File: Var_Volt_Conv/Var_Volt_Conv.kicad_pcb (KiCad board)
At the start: 6 copper layers, 101 x 65 mm, 101 parts, among them J101 Jack-DC, J102 Screw_Terminal_01x02, J103 Screw_Terminal_01x02, J201 Conn_01x05, Q101 AO3416, Q102 IRFML8244TRPBF, Q103 IRFML8244TRPBF, Q104 AO3407, Q105 AO3407, Q106 AO3407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

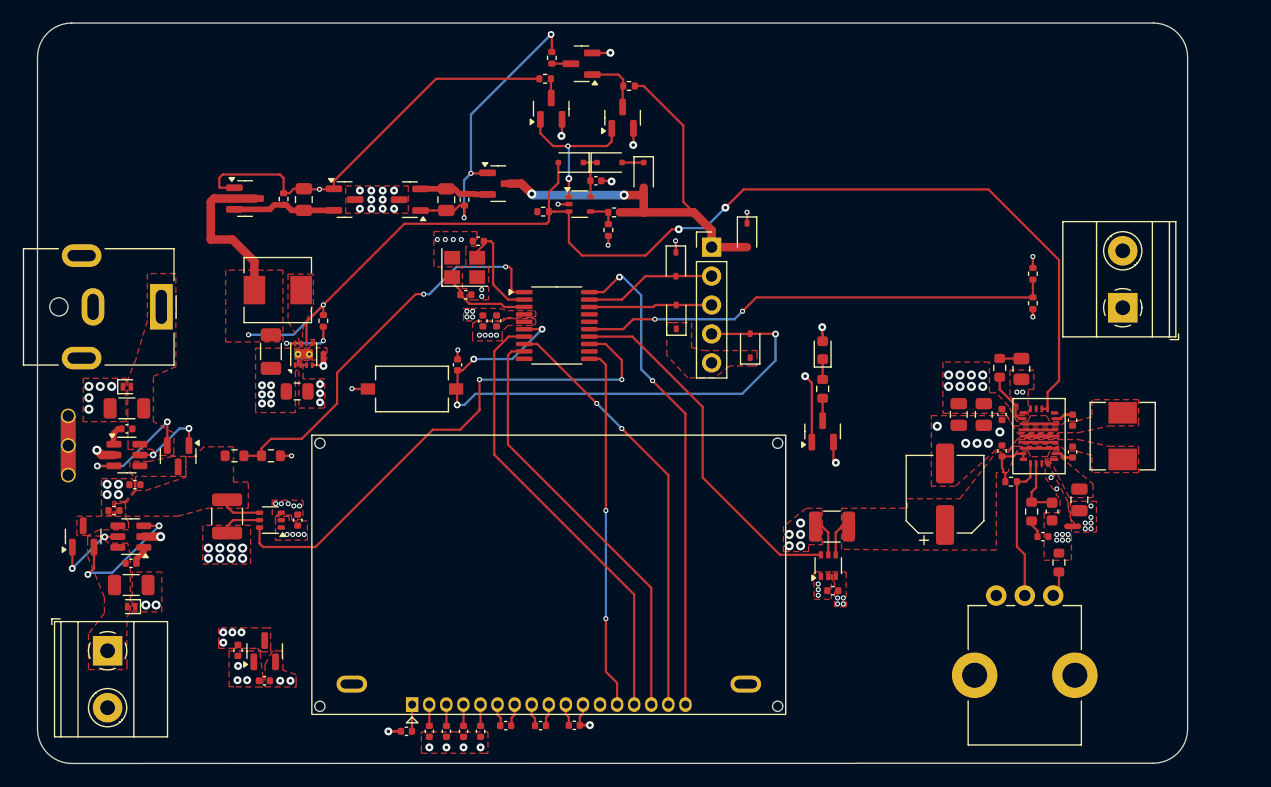
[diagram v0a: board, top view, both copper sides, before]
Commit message: Labeled subcircuits in PCB
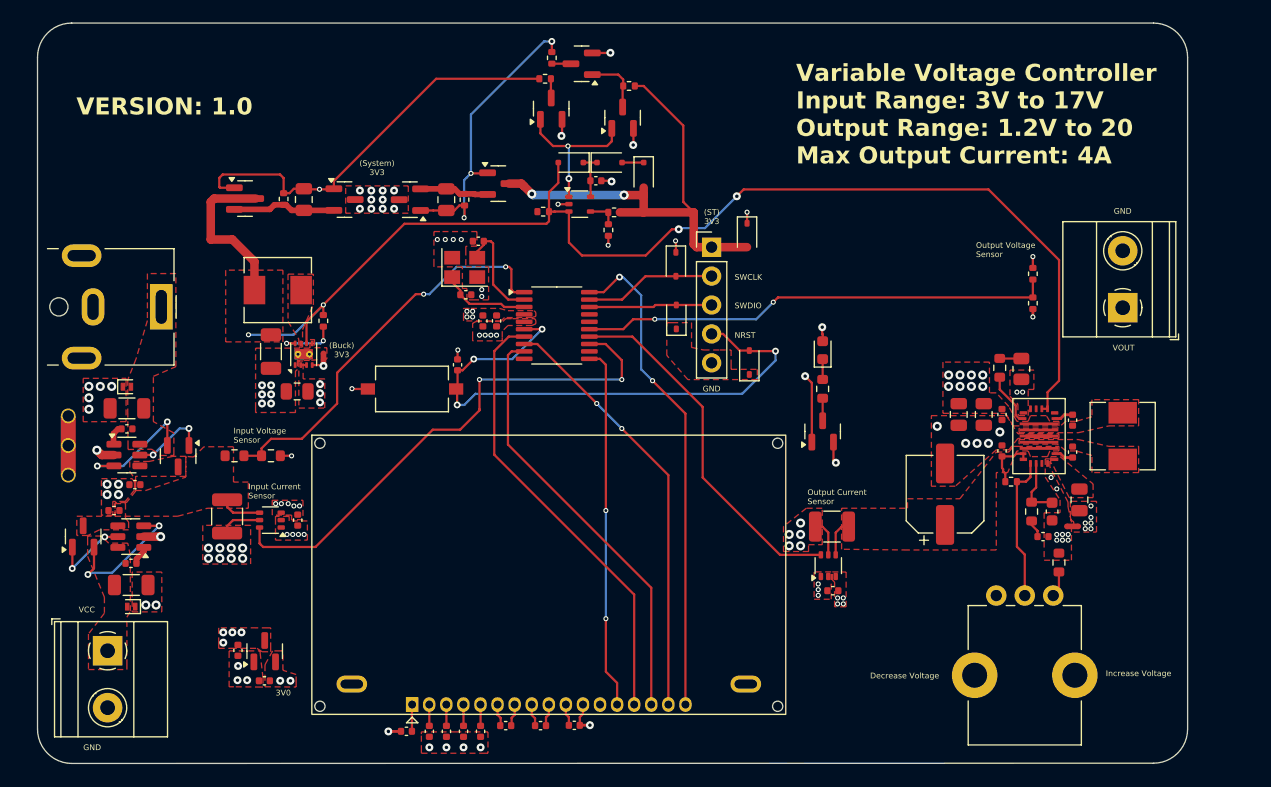
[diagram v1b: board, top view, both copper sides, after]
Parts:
- moved D201 1.48 mm to (161.5, 96.9)
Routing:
- net /[2] Microcontroller/NRST: track 51.2 -> 50.3 mm
- net /[1] Power/ST_PPM_GATE: track 27.5 -> 26.6 mm
- net ST_3V3: track 41.4 -> 42.2 mm
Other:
- board text added: "(Buck) 3V3"
- board text added: "(ST) 3V3"
- board text added: "(System) 3V3"
- board text added: "3V0"
- board text added: "Decrease Voltage"
- board text added: "GND"
- board text added: "Increase Voltage"
- board text added: "Input Current Sensor"
- board text added: "Input Voltage Sensor"
- board text added: "NRST"
- board text added: "Output Current Sensor"
- board text added: "Output Voltage Sensor"
- board text added: "SWCLK"
- board text added: "SWDIO"
- board text added: "VCC"
- board text added: "VERSION: 1.0"
- board text added: "VOUT"
- board text added: "Variable Voltage Controller Input Range: 3V to 17V Output Range: 1.2V to 20 Max Output Current: 4A"

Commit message: Added and changed size of silk-screen text
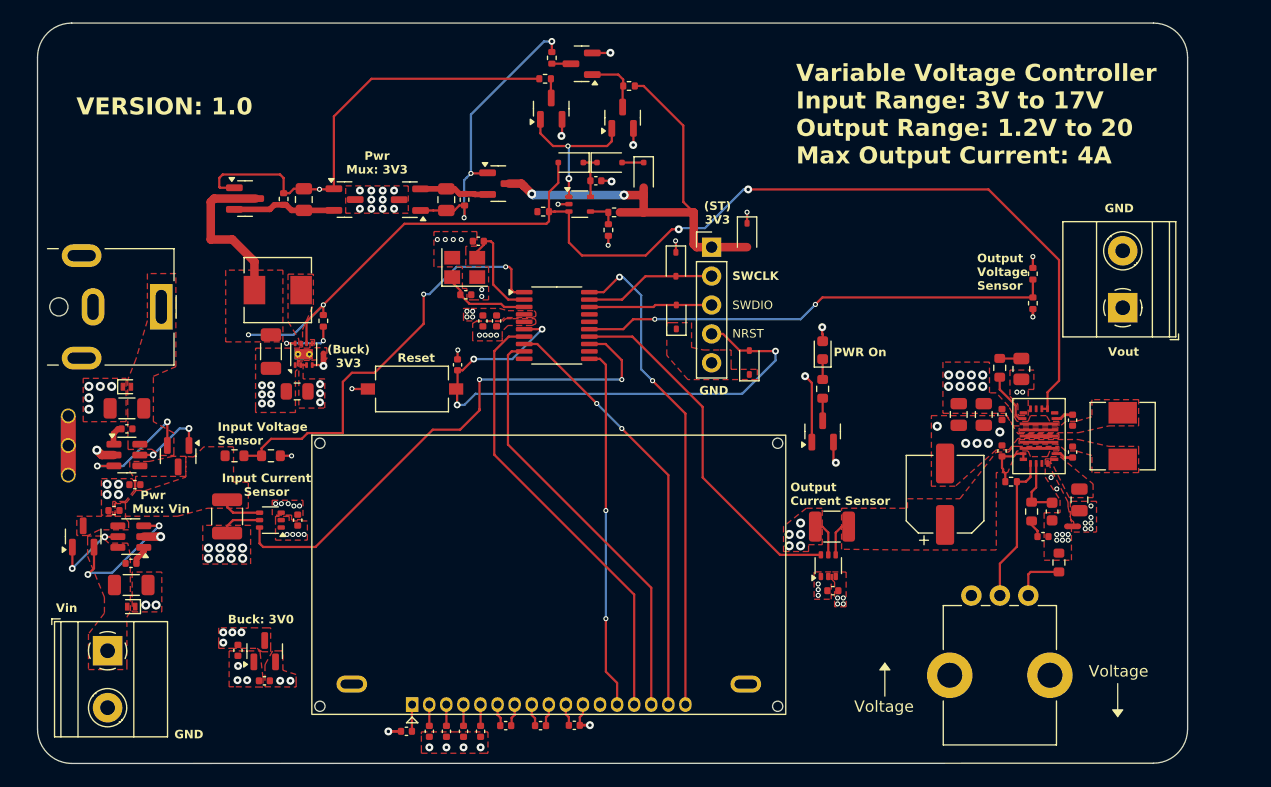
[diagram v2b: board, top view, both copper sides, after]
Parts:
- moved RV101 2.19 mm to (181.0, 117.4)
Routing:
- net /[1] Power/BUCK_PPM_GATE: track 36.4 -> 39.8 mm
- net S-INPUT_VOLTAGE: track 35.4 -> 38.0 mm
- net /[1] Power/BB_POT_R: track 2.28 -> 4.64 mm
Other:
- board text added: "Buck: 3V0"
- board text added: "PWR On"
- board text added: "Pwr Mux: 3V3"
- board text added: "Pwr Mux: Vin"
- board text added: "Reset"
- board text added: "Vin"
- board text added: "Voltage"
- board text added: "Vout"
- board text removed: "(System) 3V3"
- board text removed: "3V0"
- board text removed: "Decrease Voltage"
- board text removed: "Increase Voltage"
- board text removed: "VCC"
- board text removed: "VOUT"

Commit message: Change difference amplifieres in sensor section form 75V/V to 50V/V
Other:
- board text added: "Buck-Boost Conv."
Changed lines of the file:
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@@
 			)
 		)
-		(model "${KICAD8_3DMODEL_DIR}/LED_THT.3dshapes/LED_D3.0mm_Horizontal_O1.27mm_Z10.0mm.step"
-			(offset
-				(xyz -1.25 -10 -5)
-			)
-			(scale
-				(xyz 1 1 1)
-			)
-			(rotate
-				(xyz 90 0 0)
-			)
-		)
 	)
 	(footprint "Capacitor_SMD:C_0402_1005Metric"
@@
 		(layer "F.SilkS")
 		(effects
+			(font
+				(size 0.75 0.75)
+				(thickness 0.15)
+				(bold yes)
+			)
+			(justify left bottom)
+		)
+	)
+	(gr_text "Buck-Boost \nConv."
+		(at 189.2375 100.065 0)
+		(layer "F.SilkS")
+		(effects

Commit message: Updated schematic, C121, R112 and SW201 now use components that are still in stock on JLCPCB
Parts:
- U401, U402: value INA215BIDCKR -> INA213AIDCKR
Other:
- board text added: "Variable Voltage Controller Input Range: 3V to 17V Output Range: 1.32V to 20 Max Output Current: 4A"
- board text removed: "Variable Voltage Controller Input Range: 3V to 17V Output Range: 1.2V to 20 Max Output Current: 4A"

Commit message: Confirmed all basic components
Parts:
- R404: value 4.7K -> 4.75K
